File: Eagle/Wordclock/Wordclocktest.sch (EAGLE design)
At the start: 13 parts

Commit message: WS2812 Layout versucht
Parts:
- removed Q1: (no value), special:XTAL
- removed S+1: DS1337+, eagle-library-edeca.net-v5:DS1337+
- removed U$1: MINI-USB, eagle-library-edeca.net-v5:MINI-USB
- added C10, C11, C12, C13, C14, C15, C16, C17, C18, C19, C20, C6, C7, C8, C9: 100n, rcl:C-EUC1310
- added L10, L11, L12, L13, L14, L15, L16, L17, L18, L19, L20, L21, L22, L6, L7, L8, L9: WS2812B, adafruit:WS2812B
- C1, C2, C3, C4, C5: value (none) -> 100n
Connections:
- removed net N$21: Q1.2, S+1.X2
- removed net VCC: S+1.VCC, U$1.1
- new net +5V: C1.1, C10.1, C11.1, C12.1, C13.1, C14.1, C15.1, C16.1, C17.1, C18.1, C19.1, C2.1, C20.1, C3.1, C4.1, C5.1, C6.1, C7.1, C8.1, C9.1, L1.VDD, L10.VDD, L11.VDD, L12.VDD, L13.VDD, L14.VDD, L15.VDD, L16.VDD, L17.VDD, L18.VDD, L19.VDD, L2.VDD, L20.VDD, L21.VDD, L22.VDD, L3.VDD, L4.VDD, L5.VDD, L6.VDD, L7.VDD, L8.VDD, L9.VDD
- new net N$12: L13.DOUT, L14.DIN
- new net N$13: L14.DOUT, L15.DIN
- new net N$14: L15.DOUT, L16.DIN
- new net N$15: L16.DOUT, L17.DIN
- new net N$16: L17.DOUT, L18.DIN
- new net N$17: L18.DOUT, L19.DIN
- new net N$18: L19.DOUT, L20.DIN
- new net N$19: L20.DOUT, L21.DIN
- new net OUTROW1: L11.DOUT, L22.DOUT
- net GND: now also C10.2, C11.2, C12.2, C13.2, C14.2, C15.2, C16.2, C17.2, C18.2, C19.2, C20.2, C6.2, C7.2, C8.2, C9.2, L10.GND, L11.GND, L12.GND, L13.GND, L14.GND, L15.GND, L16.GND, L17.GND, L18.GND, L19.GND, L20.GND, L21.GND, L22.GND, L6.GND, L7.GND, L8.GND, L9.GND; no longer S+1.GND, U$1.5
- net N$10: now also L10.DOUT, L11.DIN; no longer C4.1, L4.VDD
- net N$11: now also L12.DOUT, L13.DIN; no longer C5.1, L5.VDD
- net N$20: now also L21.DOUT, L22.DIN; no longer Q1.1, S+1.X1
- net N$5: now also L6.DOUT, L7.DIN; no longer L1.DIN
- net N$6: now also L6.DIN
- net N$7: now also L7.DOUT, L8.DIN; no longer C1.1, L1.VDD
- net N$8: now also L8.DOUT, L9.DIN; no longer C2.1, L2.VDD
- net N$9: now also L10.DIN, L9.DOUT; no longer C3.1, L3.VDD

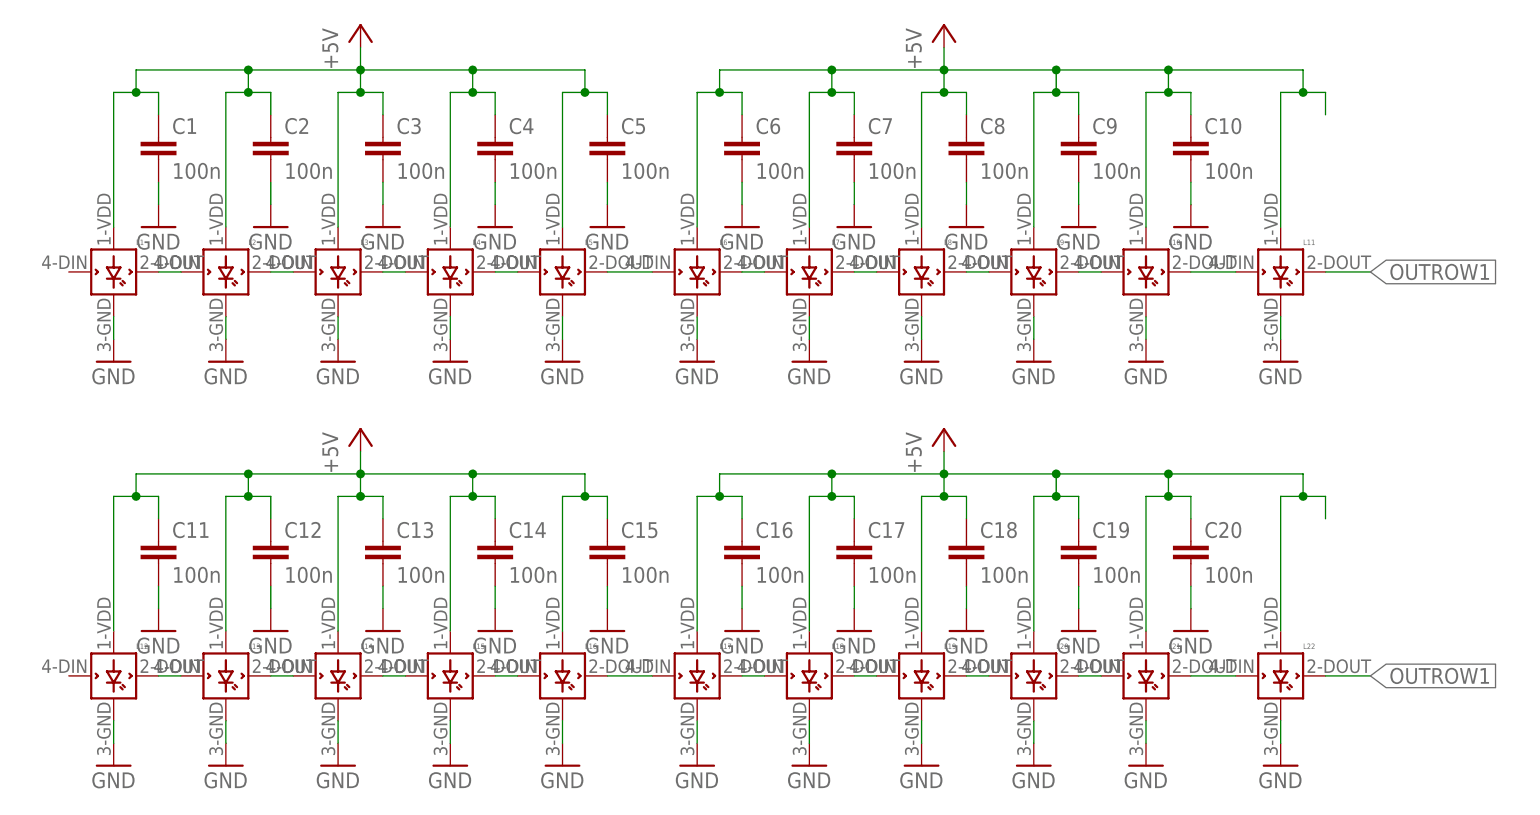
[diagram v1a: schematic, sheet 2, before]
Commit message: Frontplatte in Inkscape erstellt
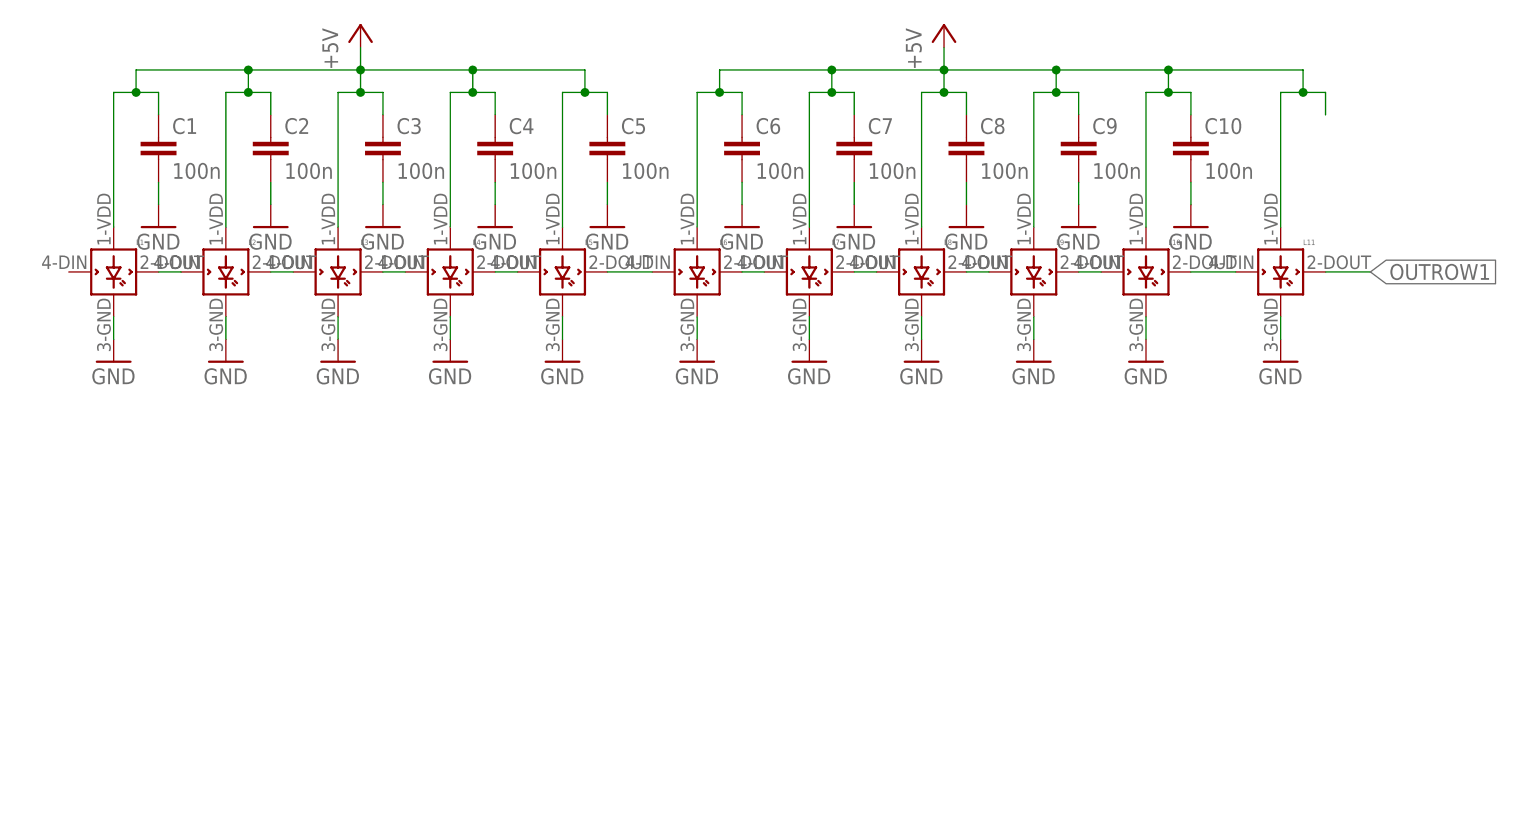
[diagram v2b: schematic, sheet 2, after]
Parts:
- removed C11, C12, C13, C14, C15, C16, C17, C18, C19, C20: 100n, rcl:C-EUC1310
- removed L12, L13, L14, L15, L16, L17, L18, L19, L20, L21, L22: WS2812B, adafruit:WS2812B
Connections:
- removed net N$11: L12.DOUT, L13.DIN
- removed net N$12: L13.DOUT, L14.DIN
- removed net N$13: L14.DOUT, L15.DIN
- removed net N$14: L15.DOUT, L16.DIN
- removed net N$15: L16.DOUT, L17.DIN
- removed net N$16: L17.DOUT, L18.DIN
- removed net N$17: L18.DOUT, L19.DIN
- removed net N$18: L19.DOUT, L20.DIN
- removed net N$19: L20.DOUT, L21.DIN
- removed net N$20: L21.DOUT, L22.DIN
- net +5V: no longer C11.1, C12.1, C13.1, C14.1, C15.1, C16.1, C17.1, C18.1, C19.1, C20.1, L12.VDD, L13.VDD, L14.VDD, L15.VDD, L16.VDD, L17.VDD, L18.VDD, L19.VDD, L20.VDD, L21.VDD, L22.VDD
- net GND: no longer C11.2, C12.2, C13.2, C14.2, C15.2, C16.2, C17.2, C18.2, C19.2, C20.2, L12.GND, L13.GND, L14.GND, L15.GND, L16.GND, L17.GND, L18.GND, L19.GND, L20.GND, L21.GND, L22.GND
- net OUTROW1: no longer L22.DOUT

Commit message: CAD Frontplattendesign eingefügt
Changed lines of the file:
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@@
-</plain>
-<instances>
-</instances>
-<busses>
-</busses>
-<nets>
-</nets>
-</sheet>
-<sheet>
-<plain>
 </plain>
 <instances>

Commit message: Wordclock Matrix gelayoutet
Matrix alle Zeilen einzeln gelautet, Zeilen sind noch nicht verbunden
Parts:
- added C11, C12, C13, C14, C15, C16, C17, C18, C19, C20, C21, C22, C23, C24, C25, C26, C27, C28, C29, C30, C31, C32, C33: 100n, rcl:C-EUC1310
- added L12, L13, L14, L15, L16, L17, L18, L19, L20, L21, L22, L23, L24, L25, L26, L27, L28, L29, L30, L31, L32, L33: WS2812B, adafruit:WS2812B
- added LED1, LED2, LED3, LED4, LED5, LED6: (no value), led:LEDCHIP-LED0603
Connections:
- new net N$11: L12.DOUT, L13.DIN
- new net N$12: L1.DIN, LED1.A
- new net N$13: L13.DOUT, L14.DIN
- new net N$14: L14.DOUT, L15.DIN
- new net N$15: L15.DOUT, L16.DIN
- new net N$16: L16.DOUT, L17.DIN
- new net N$17: L17.DOUT, L18.DIN
- new net N$18: L18.DOUT, L19.DIN
- new net N$19: L19.DOUT, L20.DIN
- new net N$20: L20.DOUT, L21.DIN
- new net N$21: L21.DOUT, L22.DIN
- new net N$22: L12.DIN, LED3.A
- new net N$23: L23.DOUT, L24.DIN
- new net N$24: L24.DOUT, L25.DIN
- new net N$25: L25.DOUT, L26.DIN
- new net N$26: L26.DOUT, L27.DIN
- new net N$27: L27.DOUT, L28.DIN
- new net N$28: L28.DOUT, L29.DIN
- new net N$29: L29.DOUT, L30.DIN
- new net N$30: L30.DOUT, L31.DIN
- new net N$31: L31.DOUT, L32.DIN
- new net N$32: L32.DOUT, L33.DIN
- new net N$33: L23.DIN, LED5.A
- new net OUTROW2: L22.DOUT, LED4.C
- new net OUTROW3: L33.DOUT, LED6.C
- net +5V: now also C11.1, C12.1, C13.1, C14.1, C15.1, C16.1, C17.1, C18.1, C19.1, C20.1, C21.1, C22.1, C23.1, C24.1, C25.1, C26.1, C27.1, C28.1, C29.1, C30.1, C31.1, C32.1, C33.1, L12.VDD, L13.VDD, L14.VDD, L15.VDD, L16.VDD, L17.VDD, L18.VDD, L19.VDD, L20.VDD, L21.VDD, L22.VDD, L23.VDD, L24.VDD, L25.VDD, L26.VDD, L27.VDD, L28.VDD, L29.VDD, L30.VDD, L31.VDD, L32.VDD, L33.VDD, LED2.A, LED4.A, LED6.A
- net GND: now also C11.2, C12.2, C13.2, C14.2, C15.2, C16.2, C17.2, C18.2, C19.2, C20.2, C21.2, C22.2, C23.2, C24.2, C25.2, C26.2, C27.2, C28.2, C29.2, C30.2, C31.2, C32.2, C33.2, L12.GND, L13.GND, L14.GND, L15.GND, L16.GND, L17.GND, L18.GND, L19.GND, L20.GND, L21.GND, L22.GND, L23.GND, L24.GND, L25.GND, L26.GND, L27.GND, L28.GND, L29.GND, L30.GND, L31.GND, L32.GND, L33.GND, LED1.C, LED3.C, LED5.C
- net OUTROW1: now also LED2.C
